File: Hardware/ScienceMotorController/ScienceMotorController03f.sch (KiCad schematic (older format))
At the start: 17 parts, among them U7 VNH5019A_E

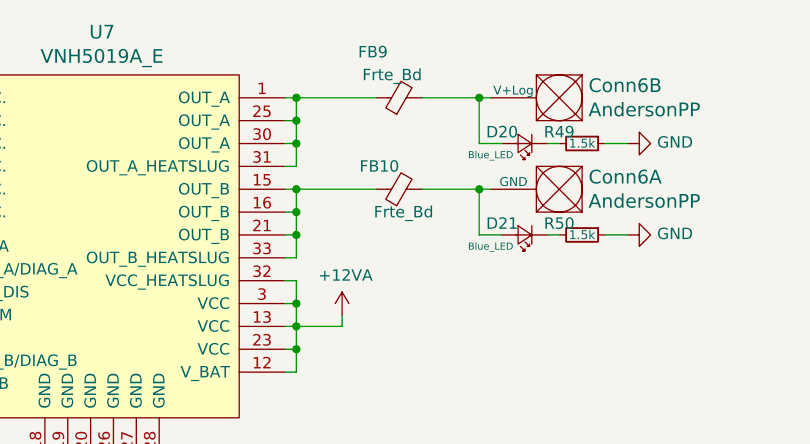
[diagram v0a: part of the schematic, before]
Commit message: assigned most of the footprints
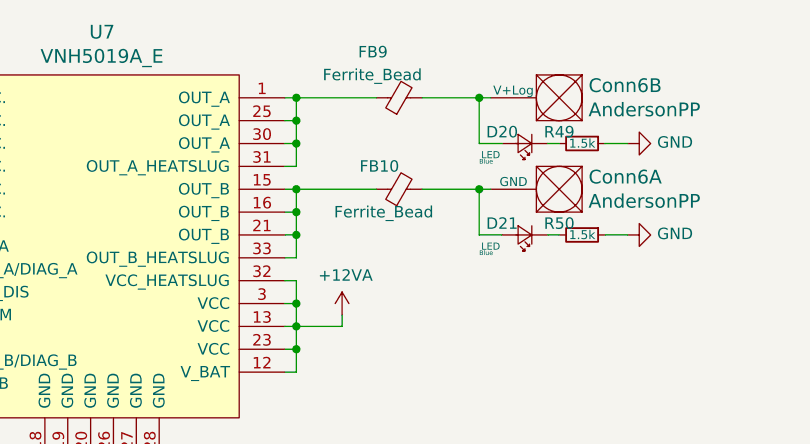
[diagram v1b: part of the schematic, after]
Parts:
- Conn6: footprint (none) -> MRDT_Connectors:Anderson_2_Vertical_Sidy_by_Side
- D19: footprint (none) -> Diode_SMD:D_0603_1608Metric_Pad1.05x0.95mm_HandSolder
- D20, D21: value Blue_LED -> LED; footprint (none) -> LED_SMD:LED_0603_1608Metric_Pad1.05x0.95mm_HandSolder
- FB10, FB9: value Frte_Bd -> Ferrite_Bead
- R42, R43, R44, R45, R46, R47, R48, R49, R50: footprint (none) -> Resistor_SMD:R_0603_1608Metric_Pad1.05x0.95mm_HandSolder
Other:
- note added: "Blue"
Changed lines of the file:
@@
 F 0 "R46" V 5350 3800 50  0000 C CNN
 F 1 "1k" V 5400 3950 50  0000 C CNN
-F 2 "" H 5400 3950 50  0001 C CNN
+F 2 "Resistor_SMD:R_0603_1608Metric_Pad1.05x0.95mm_HandSolder" H 5400 3950 50  0001 C CNN
 F 3 "~" H 5400 3950 50  0001 C CNN
 	1    5400 3950
@@
 F 0 "R43" V 4600 4200 50  0000 C CNN
 F 1 "1k" V 4700 4200 50  0000 C CNN
-F 2 "" H 4700 4200 50  0001 C CNN
+F 2 "Resistor_SMD:R_0603_1608Metric_Pad1.05x0.95mm_HandSolder" H 4700 4200 50  0001 C CNN
 F 3 "~" H 4700 4200 50  0001 C CNN
 	1    4700 4200
@@
 F 0 "D19" V 3900 4050 50  0000 R CNN
 F 1 "D_Zener_Small" V 3800 4100 50  0000 R CNN
-F 2 "" V 3850 4200 50  0001 C CNN
+F 2 "Diode_SMD:D_0603_1608Metric_Pad1.05x0.95mm_HandSolder" V 3850 4200 50  0001 C CNN
 F 3 "~" V 3850 4200 50  0001 C CNN
 	1    3850 4200
@@
 F 0 "R42" V 4300 4050 50  0000 C CNN
 F 1 "10k" V 4400 4050 50  0000 C CNN
-F 2 "" H 4400 4050 50  0001 C CNN
+F 2 "Resistor_SMD:R_0603_1608Metric_Pad1.05x0.95mm_HandSolder" H 4400 4050 50  0001 C CNN
 F 3 "~" H 4400 4050 50  0001 C CNN
 	1    4400 4050
@@
 F 0 "R47" V 5350 4000 50  0000 C CNN
 F 1 "1k" V 5400 4150 50  0000 C CNN
-F 2 "" H 5400 4150 50  0001 C CNN
+F 2 "Resistor_SMD:R_0603_1608Metric_Pad1.05x0.95mm_HandSolder" H 5400 4150 50  0001 C CNN
 F 3 "~" H 5400 4150 50  0001 C CNN
 	1    5400 4150
@@
 F 0 "R45" V 5350 3600 50  0000 C CNN
 F 1 "1k" V 5400 3750 50  0000 C CNN
-F 2 "" H 5400 3750 50  0001 C CNN
+F 2 "Resistor_SMD:R_0603_1608Metric_Pad1.05x0.95mm_HandSolder" H 5400 3750 50  0001 C CNN
 F 3 "~" H 5400 3750 50  0001 C CNN
 	1    5400 3750
@@
 F 0 "R44" V 5350 3500 50  0000 C CNN
 F 1 "1k" V 5400 3650 50  0000 C CNN
-F 2 "" H 5400 3650 50  0001 C CNN
+F 2 "Resistor_SMD:R_0603_1608Metric_Pad1.05x0.95mm_HandSolder" H 5400 3650 50  0001 C CNN
 F 3 "~" H 5400 3650 50  0001 C CNN
 	1    5400 3650
@@
 F 0 "R48" V 5350 4100 50  0000 C CNN
 F 1 "1k" V 5400 4250 50  0000 C CNN
-F 2 "" H 5400 4250 50  0001 C CNN
+F 2 "Resistor_SMD:R_0603_1608Metric_Pad1.05x0.95mm_HandSolder" H 5400 4250 50  0001 C CNN
 F 3 "~" H 5400 4250 50  0001 C CNN
 	1    5400 4250
@@
 F 0 "Conn6" H 8522 3347 60  0000 R CNN
 F 1 "AndersonPP" H 8522 3453 60  0000 R CNN
-F 2 "" H 8400 2750 60  0001 C CNN
+F 2 "MRDT_Connectors:Anderson_2_Vertical_Sidy_by_Side" H 8400 2750 60  0001 C CNN
 F 3 "" H 8400 2750 60  0001 C CNN
 	1    8550 3300
@@
 F 0 "Conn6" H 8522 2947 60  0000 R CNN
 F 1 "AndersonPP" H 8522 3053 60  0000 R CNN
-F 2 "" H 8400 2350 60  0001 C CNN
+F 2 "MRDT_Connectors:Anderson_2_Vertical_Sidy_by_Side" H 8400 2350 60  0001 C CNN
 F 3 "" H 8400 2350 60  0001 C CNN
 	2    8550 2900
@@
 AR Path="/5F7148FA/5FA34ADD/5FACB5EF" Ref="D20"  Part="1"
 F 0 "D20" H 8400 3150 50  0000 C CNN
-F 1 "Blue_LED" H 8450 3250 31  0000 C CNN
-F 2 "" V 8300 3200 50  0001 C CNN
+F 1 "LED" H 8450 3250 31  0000 C CNN
+F 2 "LED_SMD:LED_0603_1608Metric_Pad1.05x0.95mm_HandSolder" V 8300 3200 50  0001 C CNN
 F 3 "~" V 8300 3200 50  0001 C CNN
 	1    8300 3200
@@
 AR Path="/5F7148FA/5FA34ADD/5FACB5F5" Ref="D21"  Part="1"
 F 0 "D21" H 8400 3550 50  0000 C CNN
-F 1 "Blue_LED" H 8450 3650 31  0000 C CNN
-F 2 "" V 8300 3600 50  0001 C CNN
+F 1 "LED" H 8450 3650 31  0000 C CNN
+F 2 "LED_SMD:LED_0603_1608Metric_Pad1.05x0.95mm_HandSolder" V 8300 3600 50  0001 C CNN
 F 3 "~" V 8300 3600 50  0001 C CNN
 	1    8300 3600
@@
 F 0 "R50" V 8500 3500 50  0000 C CNN
 F 1 "1.5k" V 8550 3600 39  0000 C CNN
-F 2 "" H 8550 3600 50  0001 C CNN
+F 2 "Resistor_SMD:R_0603_1608Metric_Pad1.05x0.95mm_HandSolder" H 8550 3600 50  0001 C CNN
 F 3 "~" H 8550 3600 50  0001 C CNN
 	1    8550 3600
@@
 F 0 "R49" V 8500 3100 50  0000 C CNN
 F 1 "1.5k" V 8550 3200 39  0000 C CNN
-F 2 "" H 8550 3200 50  0001 C CNN
+F 2 "Resistor_SMD:R_0603_1608Metric_Pad1.05x0.95mm_HandSolder" H 8550 3200 50  0001 C CNN
 F 3 "~" H 8550 3200 50  0001 C CNN
 	1    8550 3200
@@
 AR Path="/5F7148FA/5FA34ADD/5F83E921" Ref="FB10"  Part="1"
 F 0 "FB10" V 7850 3400 50  0000 L CNN
-F 1 "Frte_Bd" V 7650 3250 50  0000 L CNN
+F 1 "Ferrite_Bead" V 7650 3250 50  0000 L CNN
 F 2 "" V 7680 3400 50  0001 C CNN
 F 3 "~" H 7750 3400 50  0001 C CNN
@@
 AR Path="/5F7148FA/5FA34ADD/5F82955C" Ref="FB9"  Part="1"
 F 0 "FB9" V 7950 3050 50  0000 L CNN
-F 1 "Frte_Bd" V 7850 2900 50  0000 L CNN
+F 1 "Ferrite_Bead" V 7850 2900 50  0000 L CNN
 F 2 "" V 7680 3000 50  0001 C CNN
 F 3 "~" H 7750 3000 50  0001 C CNN
@@
 Text HLabel 5150 4150 0    50   Output ~ 0
 3.3V
+Text Notes 8100 3300 0    20   ~ 0
+Blue
+Text Notes 8100 3700 0    20   ~ 0
+Blue
 $EndSCHEMATC

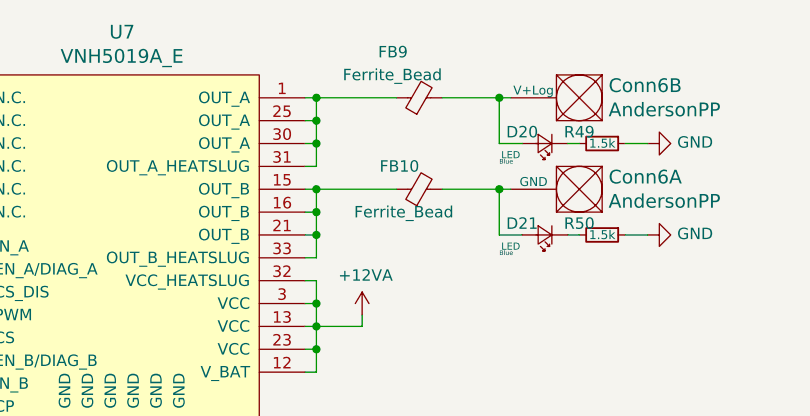
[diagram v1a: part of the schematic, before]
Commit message: finished assigning footprints, generated pcbnew
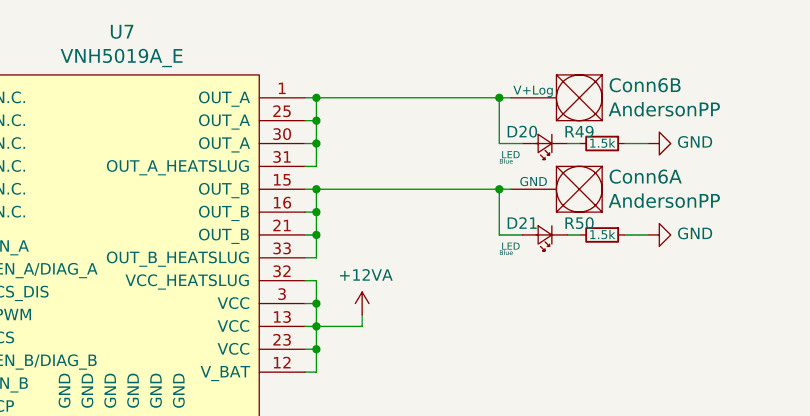
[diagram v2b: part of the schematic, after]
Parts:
- removed FB10, FB9: Ferrite_Bead, symbol Device:Ferrite_Bead_Small
- Conn6: footprint MRDT_Connectors:Anderson_2_Vertical_Sidy_by_Side -> MRDT_Connectors:Anderson_2_Horizontal_Side_by_Side
- U7: footprint (none) -> MRDT_ICs:MultiPowerSO_30
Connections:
- net at U7.1 (OUT_A), U7.25 (OUT_A), U7.30 (OUT_A)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: now also Conn6.2 (V+Log), D20.2 (A)
- net at U7.15 (OUT_B), U7.16 (OUT_B), U7.21 (OUT_B)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: now also Conn6.1 (GND), D21.2 (A)
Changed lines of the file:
@@
 F 0 "U7" H 6450 6087 60  0000 C CNN
 F 1 "VNH5019A_E" H 6450 5981 60  0000 C CNN
-F 2 "" H 5850 5700 60  0001 C CNN
+F 2 "MRDT_ICs:MultiPowerSO_30" H 5850 5700 60  0001 C CNN
 F 3 "" H 5850 5700 60  0001 C CNN
 	1    5850 4400
@@
 F 0 "Conn6" H 8522 3347 60  0000 R CNN
 F 1 "AndersonPP" H 8522 3453 60  0000 R CNN
-F 2 "MRDT_Connectors:Anderson_2_Vertical_Sidy_by_Side" H 8400 2750 60  0001 C CNN
+F 2 "MRDT_Connectors:Anderson_2_Horizontal_Side_by_Side" H 8400 2750 60  0001 C CNN
 F 3 "" H 8400 2750 60  0001 C CNN
 	1    8550 3300
@@
 F 0 "Conn6" H 8522 2947 60  0000 R CNN
 F 1 "AndersonPP" H 8522 3053 60  0000 R CNN
-F 2 "MRDT_Connectors:Anderson_2_Vertical_Sidy_by_Side" H 8400 2350 60  0001 C CNN
+F 2 "MRDT_Connectors:Anderson_2_Horizontal_Side_by_Side" H 8400 2350 60  0001 C CNN
 F 3 "" H 8400 2350 60  0001 C CNN
 	2    8550 2900
@@
 	5650 4050 4700 4050
 Connection ~ 4700 4050
-Wire Wire Line
-	7850 3000 8100 3000
-Wire Wire Line
-	7850 3400 8100 3400
 Wire Wire Line
 	8100 3200 8100 3000
@@
 Sheet 03f: Mixer Output
 $Comp
-L Device:Ferrite_Bead_Small FB?
-U 1 1 5F83E921
-P 7750 3400
-AR Path="/5F7D111E/5FA66A7C/5F83E921" Ref="FB?"  Part="1"
-AR Path="/5F908300/5F83E921" Ref="FB?"  Part="1"
-AR Path="/5F7148FA/5FA34ADD/5F83E921" Ref="FB10"  Part="1"
-F 0 "FB10" V 7850 3400 50  0000 L CNN
-F 1 "Ferrite_Bead" V 7650 3250 50  0000 L CNN
-F 2 "" V 7680 3400 50  0001 C CNN
-F 3 "~" H 7750 3400 50  0001 C CNN
-	1    7750 3400
-	0    -1   -1   0
-$EndComp
-$Comp
 L power:+12VA #PWR?
 U 1 1 5F8410BA
@@
 	1    0    0    -1
 $EndComp
-$Comp
-L Device:Ferrite_Bead_Small FB?
-U 1 1 5F82955C
-P 7750 3000
-AR Path="/5F7D111E/5FA66A7C/5F82955C" Ref="FB?"  Part="1"
-AR Path="/5F908300/5F82955C" Ref="FB?"  Part="1"
-AR Path="/5F7148FA/5FA34ADD/5F82955C" Ref="FB9"  Part="1"
-F 0 "FB9" V 7950 3050 50  0000 L CNN
-F 1 "Ferrite_Bead" V 7850 2900 50  0000 L CNN
-F 2 "" V 7680 3000 50  0001 C CNN
-F 3 "~" H 7750 3000 50  0001 C CNN
-	1    7750 3000
-	0    -1   -1   0
-$EndComp
 Connection ~ 7300 3000
 Connection ~ 7300 3400
-Wire Wire Line
-	7300 3000 7650 3000
-Wire Wire Line
-	7300 3400 7650 3400
 Text HLabel 5200 3650 0    50   Input ~ 0
 In_A_6
@@
 Text Notes 8100 3700 0    20   ~ 0
 Blue
+Wire Wire Line
+	7300 3400 8100 3400
+Wire Wire Line
+	7300 3000 8100 3000
 $EndSCHEMATC

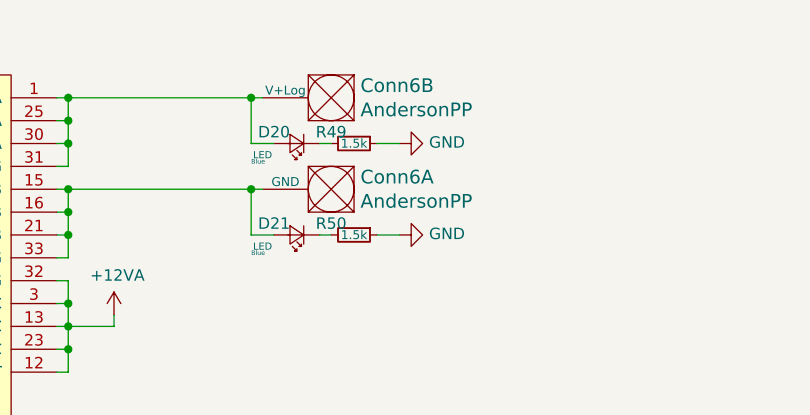
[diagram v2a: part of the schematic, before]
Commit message: running traces
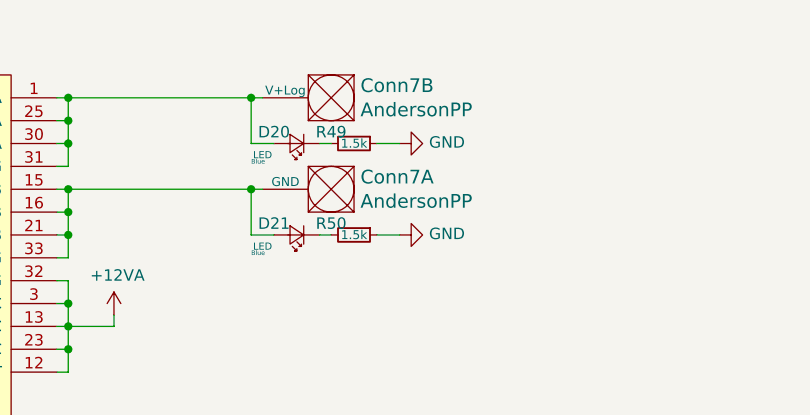
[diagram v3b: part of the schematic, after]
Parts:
- renumbered Conn6 to Conn7
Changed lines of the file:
@@
 AR Path="/5F7D111E/5FA66A7C/5FACB5D5" Ref="Conn?"  Part="1"
 AR Path="/5F908300/5FACB5D5" Ref="Conn?"  Part="1"
-AR Path="/5F7148FA/5FA34ADD/5FACB5D5" Ref="Conn6"  Part="1"
-F 0 "Conn6" H 8522 3347 60  0000 R CNN
+AR Path="/5F7148FA/5FA34ADD/5FACB5D5" Ref="Conn7"  Part="1"
+F 0 "Conn7" H 8522 3347 60  0000 R CNN
 F 1 "AndersonPP" H 8522 3453 60  0000 R CNN
 F 2 "MRDT_Connectors:Anderson_2_Horizontal_Side_by_Side" H 8400 2750 60  0001 C CNN
@@
 AR Path="/5F7D111E/5FA66A7C/5FACB5DB" Ref="Conn?"  Part="2"
 AR Path="/5F908300/5FACB5DB" Ref="Conn?"  Part="2"
-AR Path="/5F7148FA/5FA34ADD/5FACB5DB" Ref="Conn6"  Part="2"
-F 0 "Conn6" H 8522 2947 60  0000 R CNN
+AR Path="/5F7148FA/5FA34ADD/5FACB5DB" Ref="Conn7"  Part="2"
+F 0 "Conn7" H 8522 2947 60  0000 R CNN
 F 1 "AndersonPP" H 8522 3053 60  0000 R CNN
 F 2 "MRDT_Connectors:Anderson_2_Horizontal_Side_by_Side" H 8400 2350 60  0001 C CNN
